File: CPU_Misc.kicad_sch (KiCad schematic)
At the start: 1 part

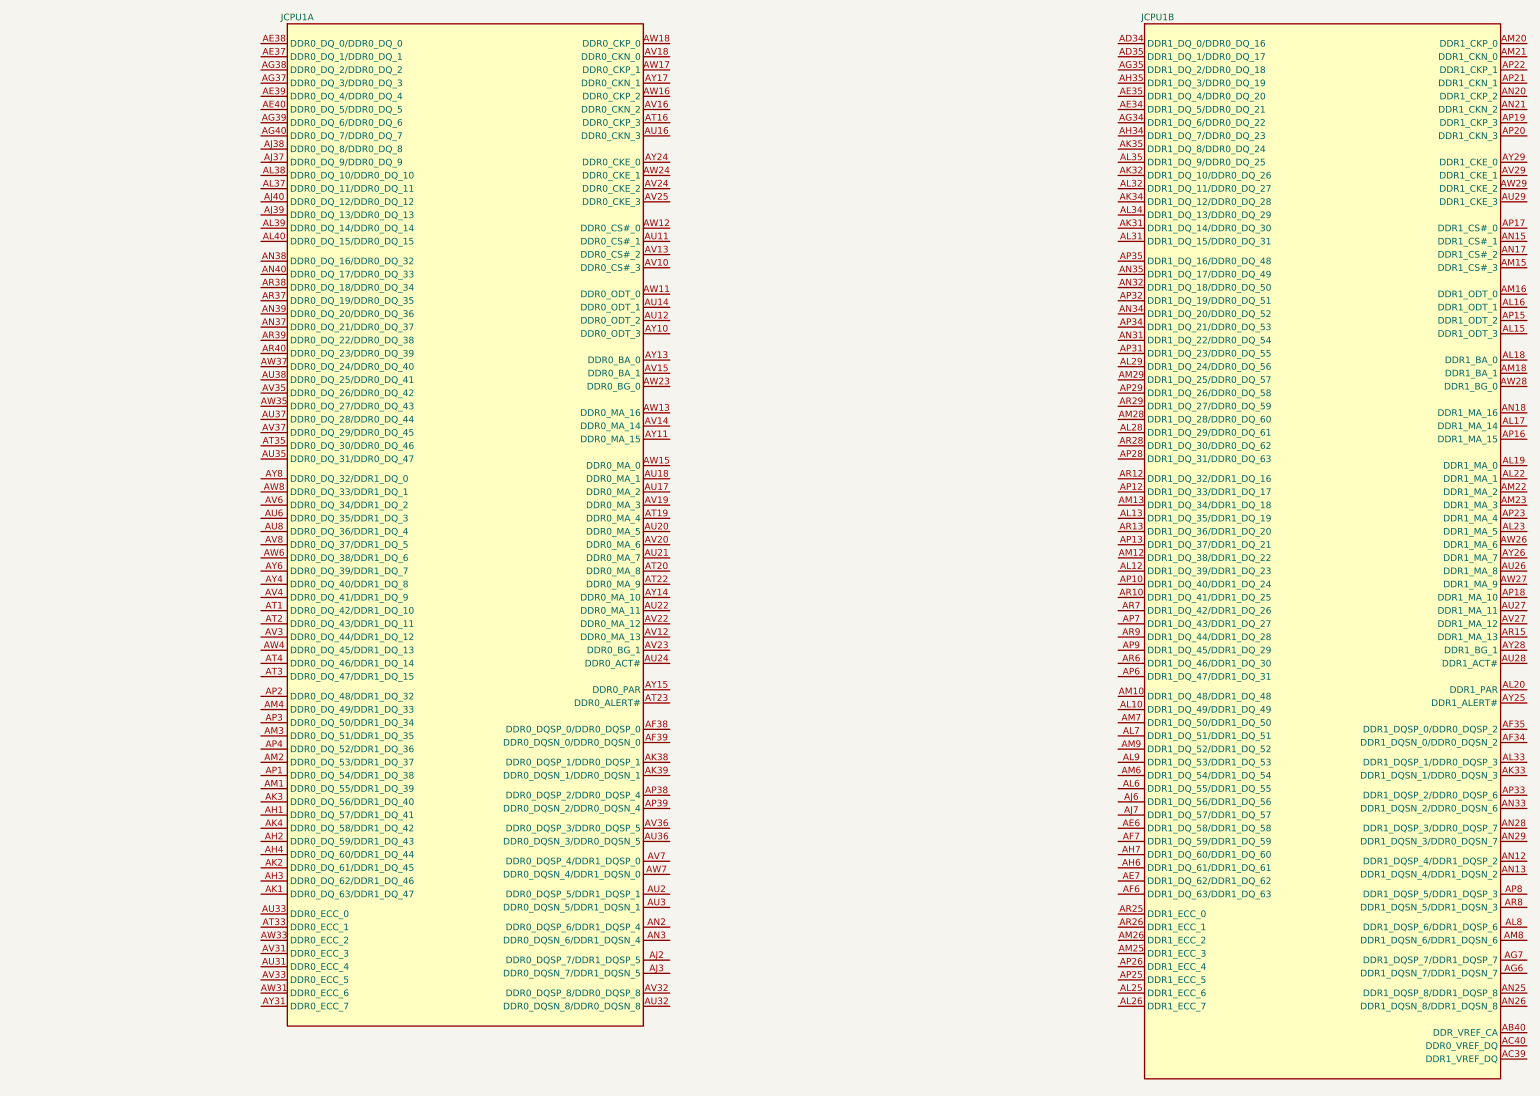
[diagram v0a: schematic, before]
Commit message: Added CPU Misc & RSVD symbol
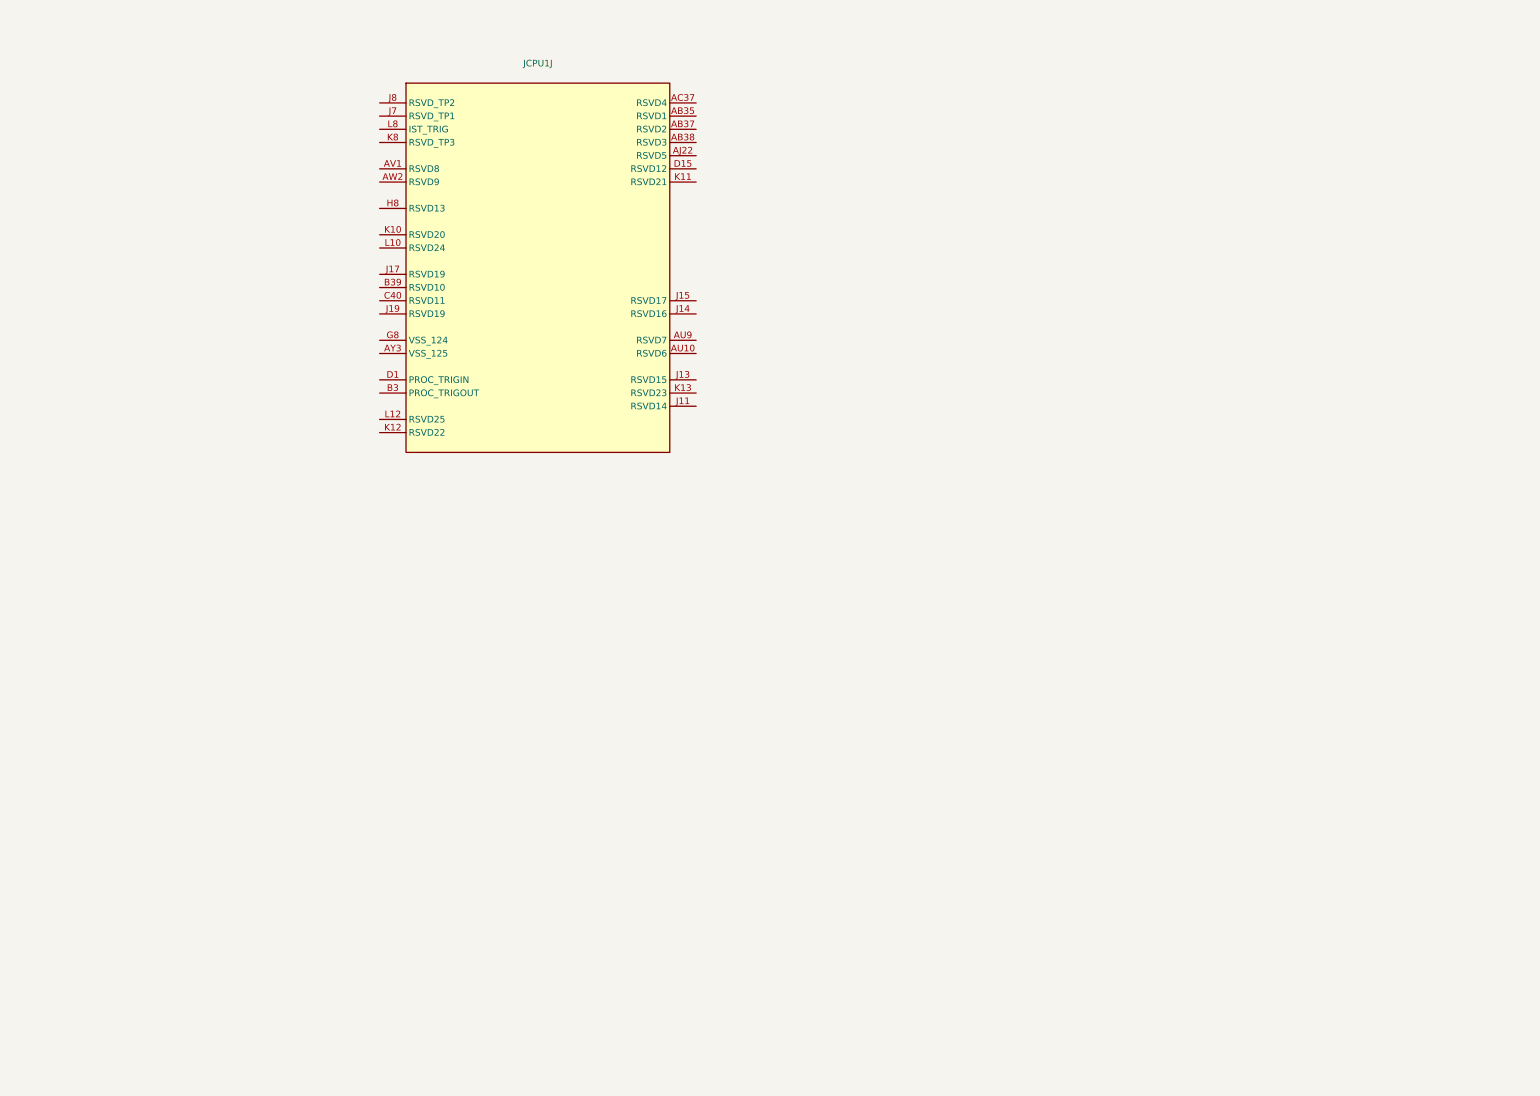
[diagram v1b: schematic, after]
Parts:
- removed JCPU1: ~, A-my-stuff:LGA-1151_L47.1-W42.5-P0.91_PE115127-4041-01H, symbol A-my-stuff:Intel_CFL_1151
- added JCPU1: ~, A-my-stuff:LGA-1151_L47.1-W42.5-P0.91_PE115127-4041-01H, symbol A-my-stuff:Intel_CFL_1151
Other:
- title: CPU Memory interface -> CPU Miscellaneous and Reserved pins

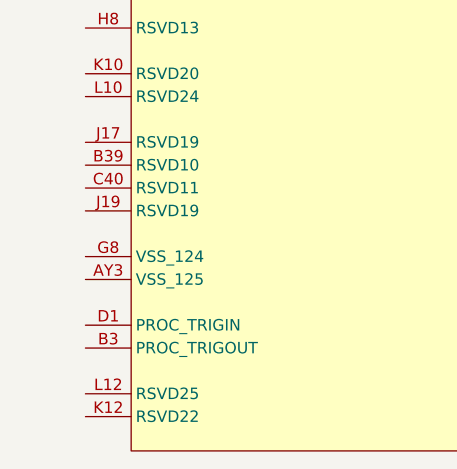
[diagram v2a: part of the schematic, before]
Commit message: Connected CPU ground
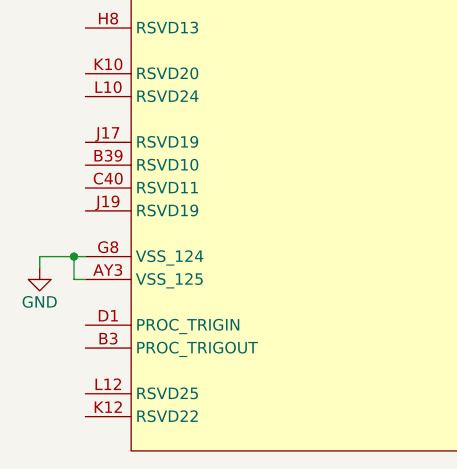
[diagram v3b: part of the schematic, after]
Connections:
- net GND: now reaches JCPU1.AY3 (VSS_125)
- net GND: now also JCPU1.G8 (VSS_124)
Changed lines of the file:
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@@
 		(company "WifiCable")
+	)
+	(junction
+		(at 90.17 101.6)
+		(diameter 0)
+		(color 0 0 0 0)
+	)
+	(wire
+		(pts
+			(xy 86.36 101.6) (xy 86.36 102.87)
+		)
+		(stroke
+			(width 0)
+			(type default)
+		)
+	)
+	(wire
+		(pts
+			(xy 86.36 101.6) (xy 90.17 101.6)
+		)
+		(stroke
+			(width 0)
+			(type default)
+		)
+	)
+	(wire
+		(pts
+			(xy 90.17 101.6) (xy 91.44 101.6)
+		)
+		(stroke
+			(width 0)
+			(type default)
+		)
+	)
+	(wire
+		(pts
+			(xy 90.17 104.14) (xy 91.44 104.14)
+		)
+		(stroke
+			(width 0)
+			(type default)
+		)
+	)
+	(wire
+		(pts
+			(xy 90.17 101.6) (xy 90.17 104.14)
+		)
+		(stroke
+			(width 0)
+			(type default)
+		)
 	)
 	(symbol
@@
 				)
 			)
+		)
+	)
+	(symbol
+		(lib_id "power:GND")
+		(at 86.36 102.87 0)
+		(unit 1)
+		(exclude_from_sim no)
+		(in_bom yes)
+		(on_board yes)
+		(dnp no)
+		(property "Reference" "#PWR04"
+			(at 86.36 109.22 0)
+			(effects
+				(font
+					(size 1.27 1.27)
+				)
+				(hide yes)
+			)
+		)
+		(property "Value" "GND"
+			(at 86.36 106.68 0)
+			(effects
+				(font
+					(size 1.27 1.27)
+				)
+			)
+		)
+		(property "Footprint" ""
+			(at 86.36 102.87 0)
+			(effects
+				(font
+					(size 1.27 1.27)
+				)
+				(hide yes)
+			)
+		)
+		(property "Datasheet" ""
+			(at 86.36 102.87 0)
+			(effects
+				(font
+					(size 1.27 1.27)
+				)
+				(hide yes)
+			)
+		)
+		(property "Description" "Power symbol creates a global label with name \"GND\" , ground"
+			(at 86.36 102.87 0)
+			(effects
+				(font
+					(size 1.27 1.27)
+				)
+				(hide yes)
+			)
+		)
+		(pin "1"
+		)
+		(instances
+			(project "Stroopwafel-LGA1151-CFL"
+				(path "/4bc771b8-eb19-46d0-8798-27231a7c6e83/e4d810de-49e6-45ae-bbfb-8cff0175b3e3"
+					(reference "#PWR04")
+					(unit 1)
+				)
+			)

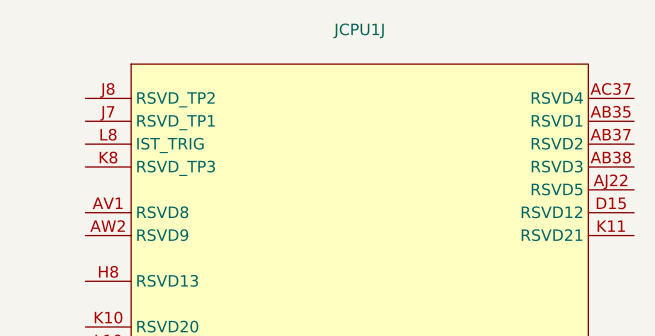
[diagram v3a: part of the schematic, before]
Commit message: Added first PCH symbol and footprint
THANKS @mothenjoyer69 so much for extracting and converting the PCH footprint from a laptop boardview ❤️
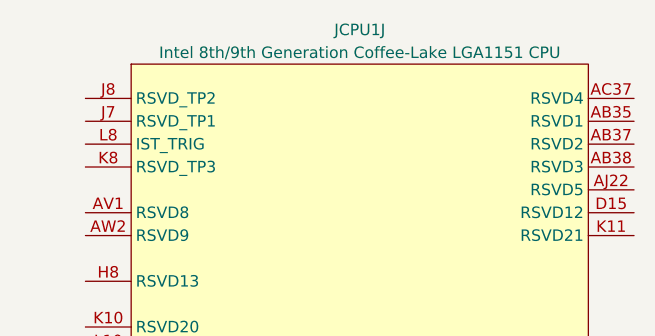
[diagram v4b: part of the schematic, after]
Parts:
- JCPU1: value ~ -> Intel 8th/9th Generation Coffee-Lake LGA1151 CPU

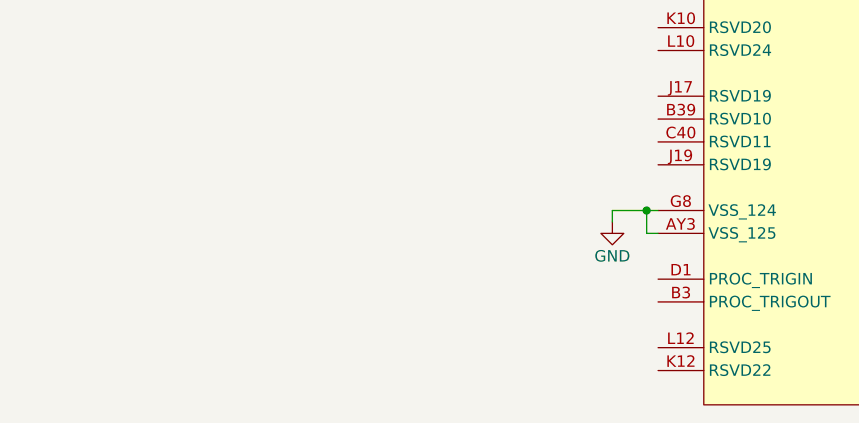
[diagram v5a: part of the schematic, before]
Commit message: Added PCH PCIe rootport/bifurcation notes
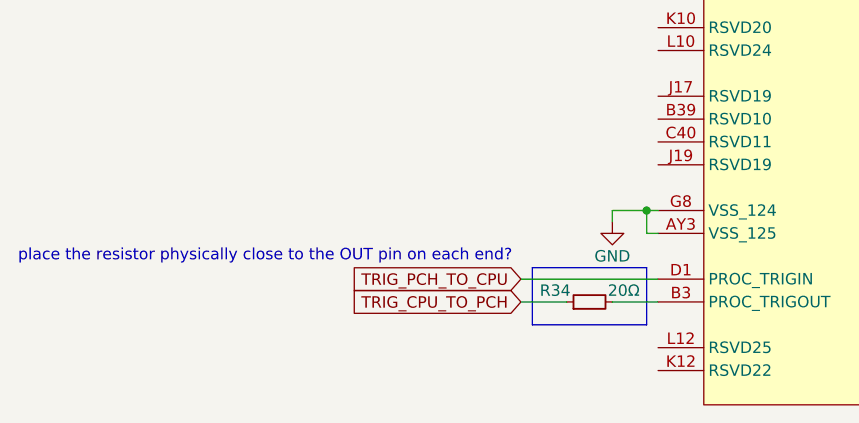
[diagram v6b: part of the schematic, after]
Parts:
- added R34: 20Ω, Resistor_SMD:R_0402_1005Metric, symbol Device:R_Small
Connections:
- net at JCPU1.B3 (PROC_TRIGOUT): now also R34.2
- net TRIG_PCH_TO_CPU: now reaches JCPU1.D1 (PROC_TRIGIN)
- new net TRIG_CPU_TO_PCH: R34.1
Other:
- note added: "place the resistor physically close to the OUT pin on each end?"
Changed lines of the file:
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@@
 		(company "WifiCable")
+	)
+	(rectangle
+		(start 77.47 107.95)
+		(end 90.17 114.3)
+		(stroke
+			(width 0)
+			(type default)
+		)
+		(fill
+			(type none)
+		)
+	)
+	(text "place the resistor physically close to the OUT pin on each end?"
+		(exclude_from_sim no)
+		(at 20.32 106.68 0)
+		(effects
+			(font
+				(size 1.27 1.27)
+			)
+			(justify left)
+		)
 	)
 	(junction
@@
 	(wire
 		(pts
+			(xy 76.2 109.22) (xy 91.44 109.22)
+		)
+		(stroke
+			(width 0)
+			(type default)
+		)
+	)
+	(wire
+		(pts
 			(xy 86.36 101.6) (xy 90.17 101.6)
 		)
@@
 	(wire
 		(pts
-			(xy 90.17 101.6) (xy 90.17 104.14)
+			(xy 86.36 111.76) (xy 91.44 111.76)
 		)
 		(stroke
 			(width 0)
 			(type default)
+		)
+	)
+	(wire
+		(pts
+			(xy 76.2 111.76) (xy 81.28 111.76)
+		)
+		(stroke
+			(width 0)
+			(type default)
+		)
+	)
+	(wire
+		(pts
+			(xy 90.17 101.6) (xy 90.17 104.14)
+		)
+		(stroke
+			(width 0)
+			(type default)
+		)
+	)
+	(global_label "TRIG_CPU_TO_PCH"
+		(shape input)
+		(at 76.2 111.76 180)
+		(fields_autoplaced yes)
+		(effects
+			(font
+				(size 1.27 1.27)
+			)
+			(justify right)
+		)
+		(property "Intersheetrefs" "${INTERSHEET_REFS}"
+			(at 61.059 111.76 0)
+			(effects
+				(font
+					(size 1.27 1.27)
+				)
+				(justify right)
+				(hide yes)
+			)
+		)
+	)
+	(global_label "TRIG_PCH_TO_CPU"
+		(shape input)
+		(at 76.2 109.22 180)
+		(fields_autoplaced yes)
+		(effects
+			(font
+				(size 1.27 1.27)
+			)
+			(justify right)
+		)
+		(property "Intersheetrefs" "${INTERSHEET_REFS}"
+			(at 61.059 109.22 0)
+			(effects
+				(font
+					(size 1.27 1.27)
+				)
+				(justify right)
+				(hide yes)
+			)
 		)
 	)
@@
 				)
 			)
+		)
+	)
+	(symbol
+		(lib_id "Device:R_Small")
+		(at 83.82 111.76 90)
+		(unit 1)
+		(exclude_from_sim no)
+		(in_bom yes)
+		(on_board yes)
+		(dnp no)
+		(property "Reference" "R34"
+			(at 80.01 110.49 90)
+			(effects
+				(font
+					(size 1.27 1.27)
+				)
+			)
+		)
+		(property "Value" "20Ω"
+			(at 87.63 110.49 90)
+			(effects
+				(font
+					(size 1.27 1.27)
+				)
+			)
+		)
+		(property "Footprint" "Resistor_SMD:R_0402_1005Metric"
+			(at 83.82 111.76 0)
+			(effects
+				(font
+					(size 1.27 1.27)
+				)
+				(hide yes)
+			)
+		)
+		(property "Datasheet" "~"
+			(at 83.82 111.76 0)
+			(effects
+				(font
+					(size 1.27 1.27)
+				)
+				(hide yes)
+			)
+		)
+		(property "Description" "Resistor, small symbol"
+			(at 83.82 111.76 0)
+			(effects
+				(font
+					(size 1.27 1.27)
+				)
+				(hide yes)
+			)
+		)
+		(pin "2"
+		)
+		(pin "1"
+		)
+		(instances
+			(project "Stroopwafel-LGA1151-CFL"
+				(path "/4bc771b8-eb19-46d0-8798-27231a7c6e83/e4d810de-49e6-45ae-bbfb-8cff0175b3e3"
+					(reference "R34")
+					(unit 1)
+				)
+			)

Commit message: stroopwafel.exe
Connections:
- net GND: no longer JCPU1.AY3 (VSS_125), JCPU1.G8 (VSS_124)
- net TRIG_PCH_TO_CPU: no longer JCPU1.D1 (PROC_TRIGIN)
- net at R34.2: no longer JCPU1.B3 (PROC_TRIGOUT)
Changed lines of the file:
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@@
 		(lib_id "A-my-stuff:Intel_CFL_1151")
 		(at 121.92 146.05 0)
-		(unit 10)
+		(unit 1)
 		(exclude_from_sim no)
 		(in_bom yes)
@@
 		(pin "J5"
 		)
-		(instances
-			(project ""
-				(path "/4bc771b8-eb19-46d0-8798-27231a7c6e83/061fe2d6-87c2-48c2-90bb-0928700512fc"
-					(reference "JCPU1")
-					(unit 10)
-				)
-				(path "/4bc771b8-eb19-46d0-8798-27231a7c6e83/e4d810de-49e6-45ae-bbfb-8cff0175b3e3"
-					(reference "JCPU1")
-					(unit 10)
-				)
-			)
-		)
 	)

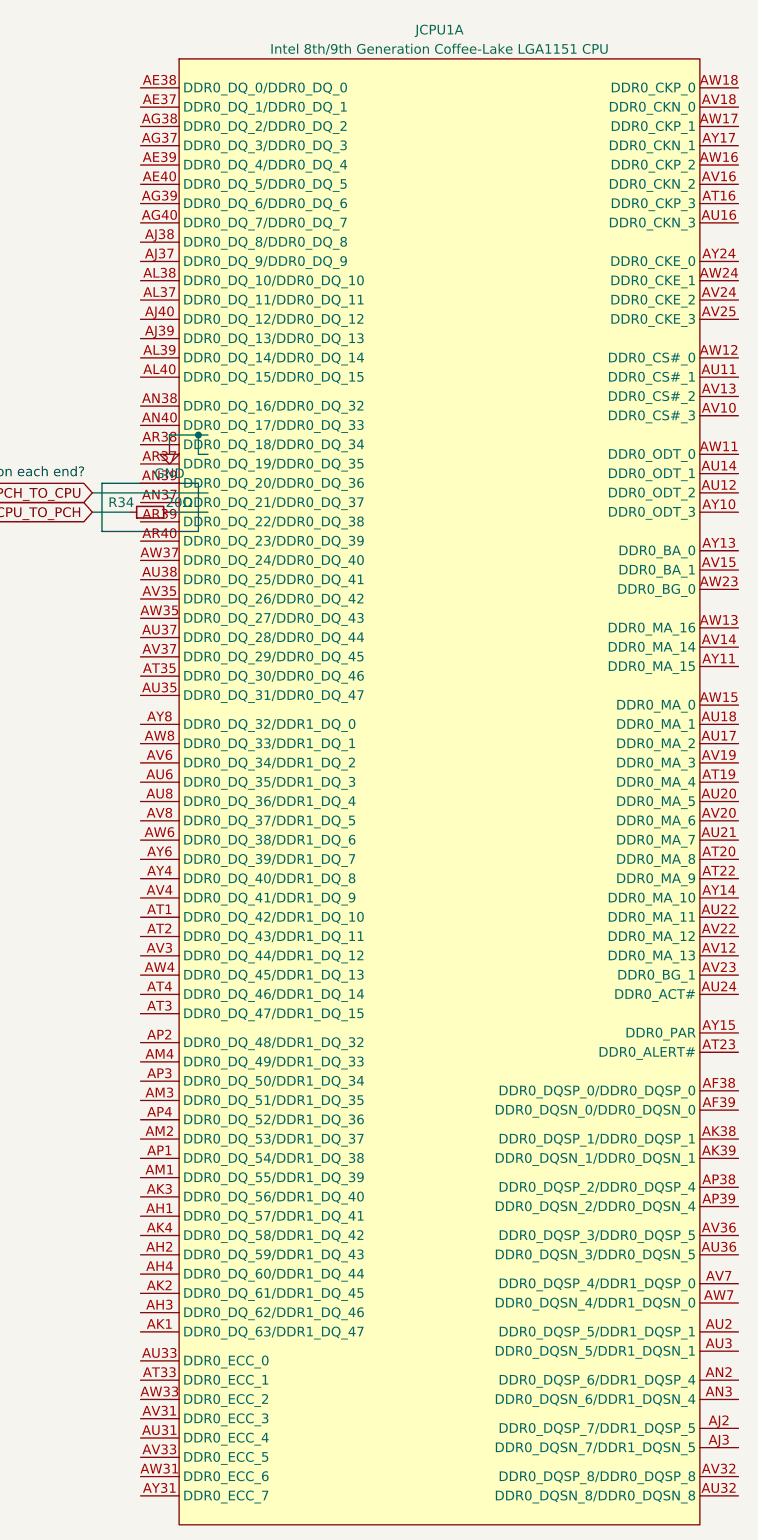
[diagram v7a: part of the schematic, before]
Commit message: Fixed entire schematic being broken
somehow every symbol with index 1 broke and updating the pcb stopped working. how does that even happen. oh well it's fixed now
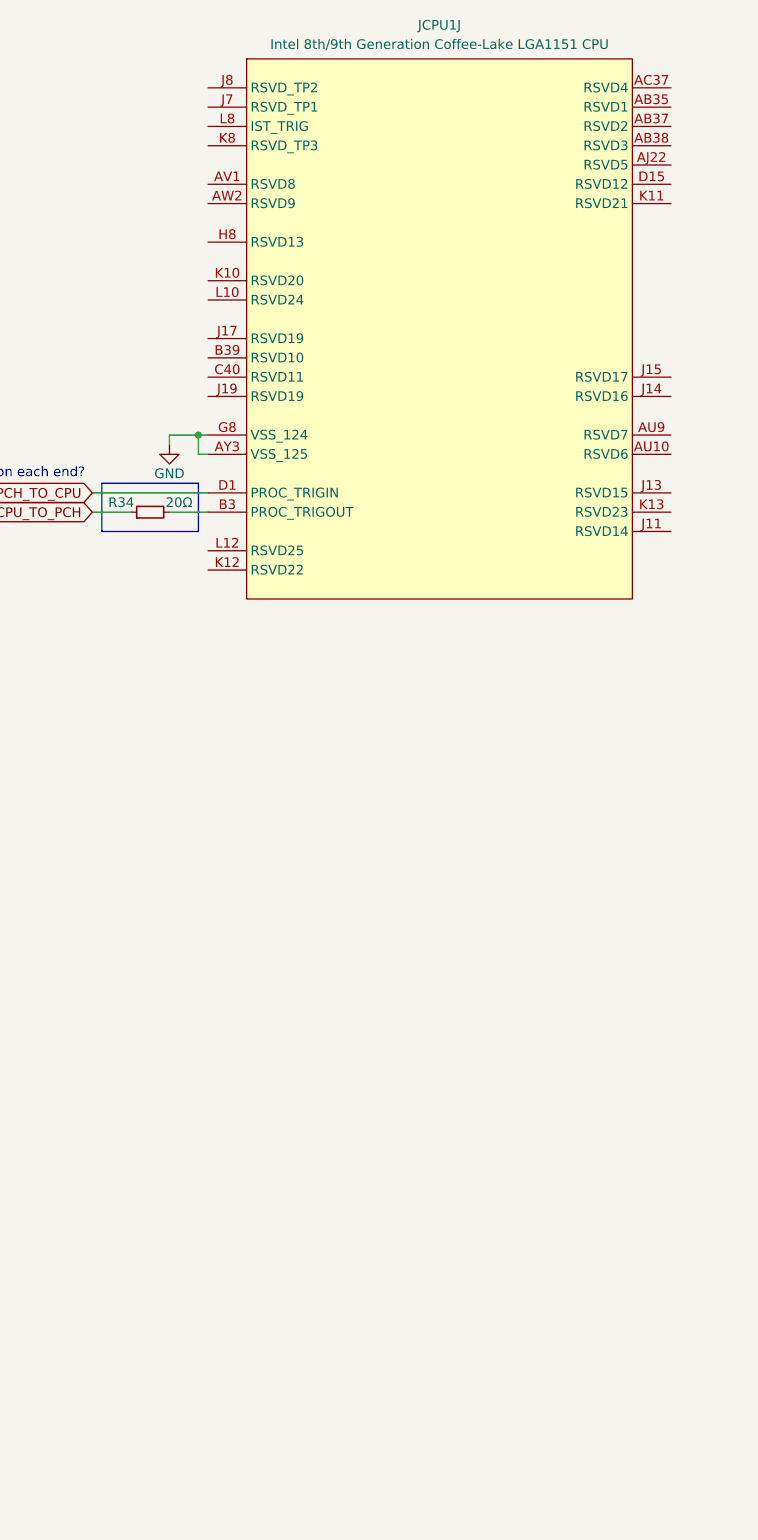
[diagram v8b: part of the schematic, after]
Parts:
- removed JCPU1: Intel 8th/9th Generation Coffee-Lake LGA1151 CPU, A-my-stuff:LGA-1151_L47.1-W42.5-P0.91_PE115127-4041-01H, symbol A-my-stuff:Intel_CFL_1151
- added JCPU1: Intel 8th/9th Generation Coffee-Lake LGA1151 CPU, A-my-stuff:LGA-1151_L47.1-W42.5-P0.91_PE115127-4041-01H, symbol A-my-stuff:Intel_CFL_1151
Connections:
- net GND: now also JCPU1.AY3 (VSS_125), JCPU1.G8 (VSS_124)
- net TRIG_PCH_TO_CPU: now also JCPU1.D1 (PROC_TRIGIN)
- net at R34.2: now also JCPU1.B3 (PROC_TRIGOUT)
